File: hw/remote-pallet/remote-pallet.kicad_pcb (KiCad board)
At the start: 2 copper layers, 90 x 90 mm, 85 parts, among them J1 Power, M0 E-MATCH, M1 E-MATCH, M2 E-MATCH, M3 E-MATCH, M4 E-MATCH, M5 E-MATCH, M6 E-MATCH, M7 E-MATCH, Q1 EMatch Test, Q10 Q_PMOS_DGS, Q11 Q_NMOS_DGS, Q12 Q_PMOS_DGS, Q13 Q_NMOS_DGS, Q14 Q_PMOS_DGS, Q15 Q_NMOS_DGS, Q16 Q_PMOS_DGS, Q17 Q_NMOS_DGS, Q2 Q_PMOS_DGS, Q3 Q_NMOS_DGS, Q4 Q_PMOS_DGS, Q5 Q_NMOS_DGS, Q6 Q_PMOS_DGS, Q7 Q_NMOS_DGS, Q8 Q_PMOS_DGS, Q9 Q_NMOS_DGS, SW1 Power, SW2 Arm Hardware, U1 Photon Power, U2 PHOTON, U3 Armed Sense

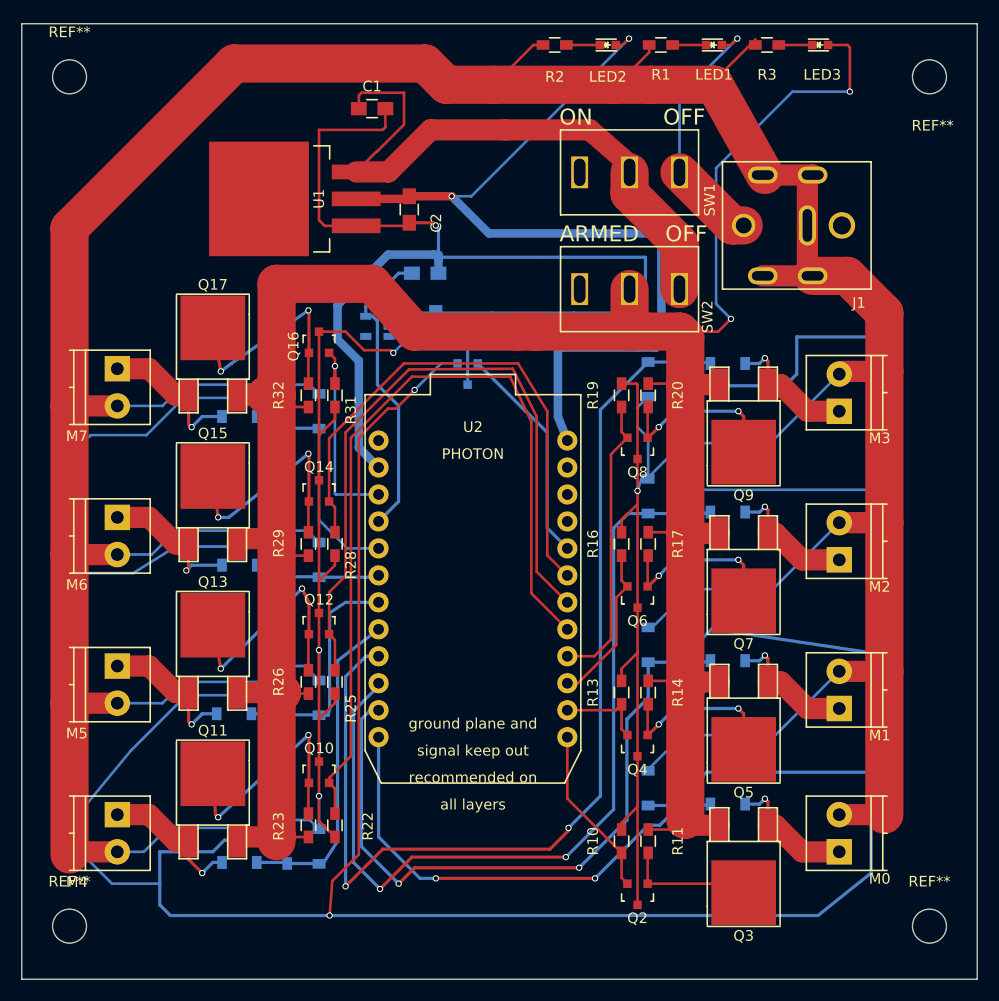
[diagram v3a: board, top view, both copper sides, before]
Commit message: adding graphic and small updates to PCB
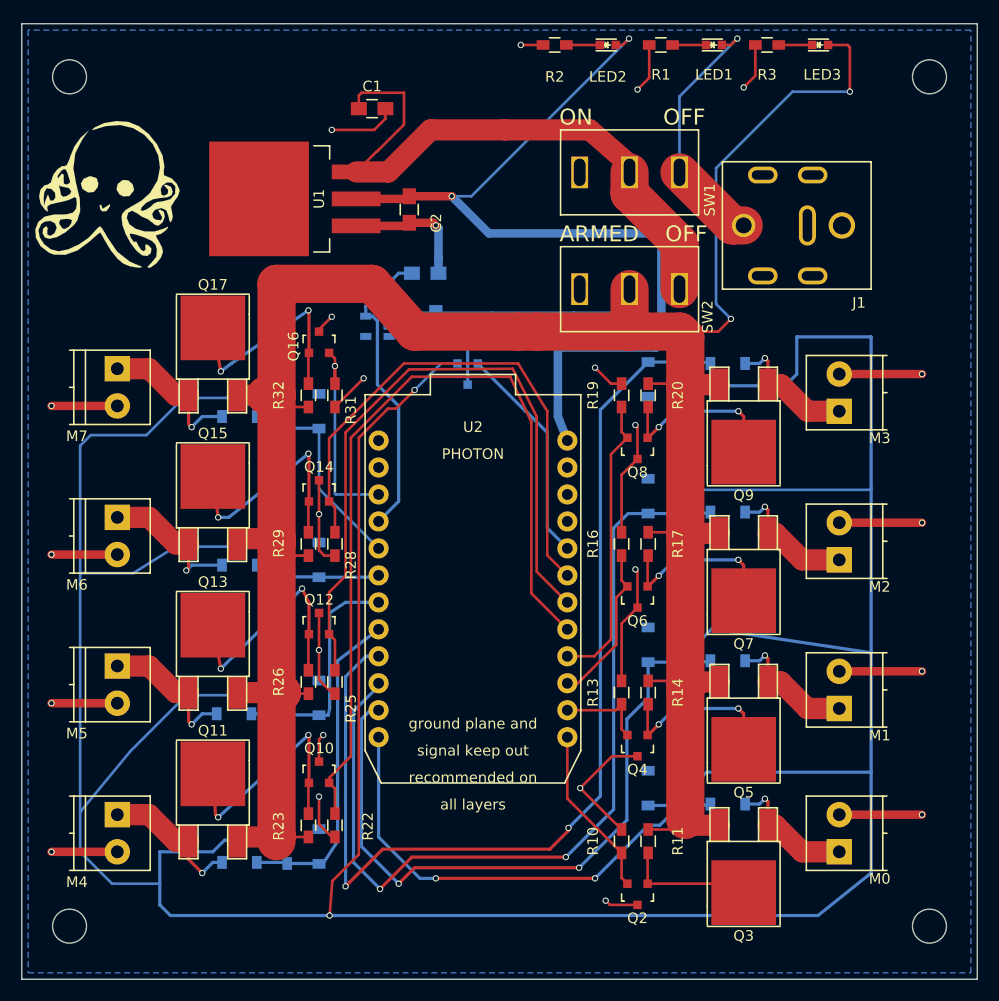
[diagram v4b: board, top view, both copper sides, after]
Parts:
- added G***: LOGO, octopus:octopus, F.Cu at (99.8, 66.2)
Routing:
- net GND: track 678.2 -> 158.5 mm, vias 5 -> 24
- net Sense7: track 21.7 -> 19.9 mm
- added copper zone on B.Cu, net GND

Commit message: updating pcb and adding part numbers for digikey
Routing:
- net GND: track 158.5 -> 234.7 mm, vias 24 -> 32
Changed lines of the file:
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@@
     (thickness 1.6)
     (drawings 10)
-    (tracks 567)
+    (tracks 597)
     (zones 0)
     (modules 86)
@@
   (segment (start 121.5 83.9) (end 121.5 81.55076) (width 0.25) (layer F.Cu) (net 30))
   (segment (start 121.5 81.55076) (end 120.95 81.00076) (width 0.25) (layer F.Cu) (net 30))
+  (segment (start 169 83) (end 169 80.1) (width 0.8) (layer F.Cu) (net 31) (status 400000))
+  (via (at 176.8 79.8) (size 0.6) (drill 0.4) (layers F.Cu B.Cu) (net 31))
+  (segment (start 169.3 79.8) (end 176.8 79.8) (width 0.8) (layer F.Cu) (net 31))
+  (segment (start 169 80.1) (end 169.3 79.8) (width 0.8) (layer F.Cu) (net 31))
+  (segment (start 169 97) (end 169 94.4) (width 0.8) (layer F.Cu) (net 31) (status 400000))
+  (via (at 176.8 94.3) (size 0.6) (drill 0.4) (layers F.Cu B.Cu) (net 31))
+  (segment (start 169.1 94.3) (end 176.8 94.3) (width 0.8) (layer F.Cu) (net 31))
+  (segment (start 169 94.4) (end 169.1 94.3) (width 0.8) (layer F.Cu) (net 31))
+  (segment (start 169 111) (end 169 107.5) (width 0.8) (layer F.Cu) (net 31) (status 400000))
+  (via (at 176.8 107.2) (size 0.6) (drill 0.4) (layers F.Cu B.Cu) (net 31))
+  (segment (start 169.3 107.2) (end 176.8 107.2) (width 0.8) (layer F.Cu) (net 31))
+  (segment (start 169 107.5) (end 169.3 107.2) (width 0.8) (layer F.Cu) (net 31))
+  (segment (start 169 124.5) (end 169 122.2) (width 0.8) (layer F.Cu) (net 31) (status 400000))
+  (via (at 176.8 121.9) (size 0.6) (drill 0.4) (layers F.Cu B.Cu) (net 31))
+  (segment (start 169.3 121.9) (end 176.8 121.9) (width 0.8) (layer F.Cu) (net 31))
+  (segment (start 169 122.2) (end 169.3 121.9) (width 0.8) (layer F.Cu) (net 31))
+  (segment (start 101 86) (end 101 88.1) (width 0.8) (layer F.Cu) (net 31) (status 400000))
+  (via (at 94.8 88.3) (size 0.6) (drill 0.4) (layers F.Cu B.Cu) (net 31))
+  (segment (start 100.8 88.3) (end 94.8 88.3) (width 0.8) (layer F.Cu) (net 31))
+  (segment (start 101 88.1) (end 100.8 88.3) (width 0.8) (layer F.Cu) (net 31))
+  (segment (start 101 100) (end 101 102.5) (width 0.8) (layer F.Cu) (net 31) (status 400000))
+  (via (at 94.8 102.4) (size 0.6) (drill 0.4) (layers F.Cu B.Cu) (net 31))
+  (segment (start 100.9 102.4) (end 94.8 102.4) (width 0.8) (layer F.Cu) (net 31))
+  (segment (start 101 102.5) (end 100.9 102.4) (width 0.8) (layer F.Cu) (net 31))
+  (segment (start 101 114) (end 101 116) (width 0.8) (layer F.Cu) (net 31) (status 400000))
+  (via (at 94.8 116) (size 0.6) (drill 0.4) (layers F.Cu B.Cu) (net 31))
+  (segment (start 101 116) (end 94.8 116) (width 0.8) (layer F.Cu) (net 31))
+  (segment (start 101 128) (end 101 129.8) (width 0.8) (layer F.Cu) (net 31) (status 400000))
+  (via (at 94.8 129.8) (size 0.6) (drill 0.4) (layers F.Cu B.Cu) (net 31))
+  (segment (start 101 129.8) (end 94.8 129.8) (width 0.8) (layer F.Cu) (net 31))
+  (segment (start 101 128) (end 94.8 128) (width 0.8) (layer F.Cu) (net 31))
+  (via (at 94.8 128) (size 0.6) (drill 0.4) (layers F.Cu B.Cu) (net 31))
   (segment (start 101 86) (end 94.8 86) (width 0.8) (layer F.Cu) (net 31))
   (via (at 94.8 86) (size 0.6) (drill 0.4) (layers F.Cu B.Cu) (net 31))
@@
   (segment (start 101 114) (end 94.8 114) (width 0.8) (layer F.Cu) (net 31))
   (via (at 94.8 114) (size 0.6) (drill 0.4) (layers F.Cu B.Cu) (net 31))
-  (segment (start 101 128) (end 94.8 128) (width 0.8) (layer F.Cu) (net 31))
-  (via (at 94.8 128) (size 0.6) (drill 0.4) (layers F.Cu B.Cu) (net 31))
   (segment (start 120 79.00178) (end 120 78.8) (width 0.25) (layer F.Cu) (net 31))
   (segment (start 120 78.8) (end 121.2 77.6) (width 0.25) (layer F.Cu) (net 31))

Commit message: updating schematic and PCB
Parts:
- added C5: 100pF, Capacitors_SMD:C_0805_HandSoldering, F.Cu at (152.8, 117.4)
- 3.3V1: renamed from LED2; value 3.3 -> Yellow
- Armed1: renamed from LED3; value Armed -> Green
- Battery1: renamed from LED1; value Battery -> Red
- C3: value 0.47uF -> 10uF; moved to F.Cu
- C4, Q1, U3: moved to F.Cu
- Q10, Q12, Q14, R22, R23, R25, R26, R28, R29: moved to B.Cu
- Q11, Q13, Q15, Q17, Q3, Q5, Q7, Q9: value Q_NMOS_DGS -> Q_NMOS_GDS
- moved R2 86.8 mm to (168.2, 134.8), turned to 0 degrees
- moved R1 86.3 mm to (168.2, 136.8), turned to 0 degrees
- moved J1 85.5 mm to (121.8, 138.2), turned to 90 degrees
- moved Battery1 85.1 mm to (164.4, 136.8), turned to 180 degrees
- moved 3.3V1 84.6 mm to (164.4, 134.8), turned to 180 degrees
- moved R3 81.0 mm to (168.2, 132.8), turned to 0 degrees
- moved Armed1 80.8 mm to (164.4, 132.8), turned to 180 degrees
- moved SW1 69.1 mm to (134.8, 131.6), turned to 180 degrees
- moved G*** 64.8 mm to (49.0, 106.4)
- moved Q2 62.1 mm to (147.4, 70.0), turned to 270 degrees
- moved R23 61.5 mm to (151.4, 73.2), turned to 180 degrees
- moved R22 58.2 mm to (151.4, 75.6), turned to 0 degrees
- moved C1 58.1 mm to (152.8, 109.0), turned to 270 degrees
- moved R10 58.1 mm to (151.4, 69.0), turned to 0 degrees
- moved SW2 56.7 mm to (145.6, 131.6), turned to 180 degrees
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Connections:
- Q1 pad 1: VCCsense -> SenseSwitch
- Q1 pad 2: SenseSwitch -> 3.3V
- Q1 pad 3: 3.3V -> VCCsense
- Q10 pad 1: Net-(Q10-Pad1) -> Fire4
- Q10 pad 2: Fire4 -> GND
- Q10 pad 3: GND -> Net-(Q10-Pad3)
- Q11 pad 1: /ematch-4/EMATCH_VCC -> Net-(Q10-Pad3)
- Q11 pad 2: Net-(Q10-Pad1) -> /ematch-4/EMATCH_VCC
- Q12 pad 1: Net-(Q12-Pad1) -> Fire5
- Q12 pad 2: Fire5 -> GND
- Q12 pad 3: GND -> Net-(Q12-Pad3)
- Q13 pad 1: /ematch-5/EMATCH_VCC -> Net-(Q12-Pad3)
- Q13 pad 2: Net-(Q12-Pad1) -> /ematch-5/EMATCH_VCC
- Q14 pad 1: Net-(Q14-Pad1) -> Fire6
- Q14 pad 2: Fire6 -> GND
- Q14 pad 3: GND -> Net-(Q14-Pad3)
- Q15 pad 1: /ematch-6/EMATCH_VCC -> Net-(Q14-Pad3)
- Q15 pad 2: Net-(Q14-Pad1) -> /ematch-6/EMATCH_VCC
- Q16 pad 1: Net-(Q16-Pad1) -> Fire7
- Q16 pad 2: Fire7 -> GND
- Q16 pad 3: GND -> Net-(Q16-Pad3)
- Q17 pad 1: /ematch-7/EMATCH_VCC -> Net-(Q16-Pad3)
- Q17 pad 2: Net-(Q16-Pad1) -> /ematch-7/EMATCH_VCC
- Q2 pad 1: Net-(Q2-Pad1) -> Fire0
- Q2 pad 2: Fire0 -> GND
- Q2 pad 3: GND -> Net-(Q2-Pad3)
- Q3 pad 1: /ematch-0/EMATCH_VCC -> Net-(Q2-Pad3)
- Q3 pad 2: Net-(Q2-Pad1) -> /ematch-0/EMATCH_VCC
- Q4 pad 1: Net-(Q4-Pad1) -> Fire1
- Q4 pad 2: Fire1 -> GND
- Q4 pad 3: GND -> Net-(Q4-Pad3)
- Q5 pad 1: /ematch-1/EMATCH_VCC -> Net-(Q4-Pad3)
- Q5 pad 2: Net-(Q4-Pad1) -> /ematch-1/EMATCH_VCC
- Q6 pad 1: Net-(Q6-Pad1) -> Fire2
- Q6 pad 2: Fire2 -> GND
- Q6 pad 3: GND -> Net-(Q6-Pad3)
- Q7 pad 1: /ematch-2/EMATCH_VCC -> Net-(Q6-Pad3)
- Q7 pad 2: Net-(Q6-Pad1) -> /ematch-2/EMATCH_VCC
- Q8 pad 1: Net-(Q8-Pad1) -> Fire3
- Q8 pad 2: Fire3 -> GND
- Q8 pad 3: GND -> Net-(Q8-Pad3)
- Q9 pad 1: /ematch-3/EMATCH_VCC -> Net-(Q8-Pad3)
- Q9 pad 2: Net-(Q8-Pad1) -> /ematch-3/EMATCH_VCC
- R11 pad 2: Net-(Q2-Pad1) -> Net-(Q2-Pad3)
- R14 pad 2: Net-(Q4-Pad1) -> Net-(Q4-Pad3)
- R17 pad 2: Net-(Q6-Pad1) -> Net-(Q6-Pad3)
- R20 pad 2: Net-(Q8-Pad1) -> Net-(Q8-Pad3)
- R23 pad 2: Net-(Q10-Pad1) -> Net-(Q10-Pad3)
- R26 pad 2: Net-(Q12-Pad1) -> Net-(Q12-Pad3)
- R29 pad 2: Net-(Q14-Pad1) -> Net-(Q14-Pad3)
- R32 pad 2: Net-(Q16-Pad1) -> Net-(Q16-Pad3)
- U2 pad 13: Fire0 -> Fire6
- U2 pad 14: Fire1 -> Fire5
- U2 pad 15: Fire2 -> Fire4
- U2 pad 16: Fire3 -> Fire0
- U2 pad 17: Fire4 -> Fire1
- U2 pad 18: Fire5 -> Fire2
- U2 pad 19: Fire6 -> Fire3
- U3 pad 3: (no net) -> /ematch-0/VCC
- U3 pad 4: (no net) -> Net-(C5-Pad1)
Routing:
- net VCCsense: track 385.7 -> 23.8 mm, vias 2 -> 8
- net GND: track 234.7 -> 0.00 mm, vias 32 -> 0
- net Net-(Q10-Pad3): track 0.00 -> 96.5 mm, vias 0 -> 1
- net Sense3: track 100.0 -> 13.3 mm, vias 2 -> 0
- net Net-(Q12-Pad3): track 0.00 -> 76.4 mm, vias 0 -> 1
- net 3.3V: track 95.8 -> 169.4 mm, vias 2 -> 1
- net Net-(Q14-Pad3): track 0.00 -> 70.8 mm, vias 0 -> 1
- net Sense2: track 82.7 -> 13.6 mm, vias 2 -> 0
- net Fire4: track 79.5 -> 11.4 mm
- net Net-(Q2-Pad3): track 0.00 -> 61.2 mm, vias 0 -> 2
- net Fire5: track 65.2 -> 9.93 mm
- net Sense1: track 64.5 -> 13.4 mm, vias 2 -> 0
- net Net-(Q4-Pad3): track 0.00 -> 49.5 mm, vias 0 -> 2
- net Fire6: track 51.3 -> 8.82 mm
- net Net-(Q6-Pad3): track 0.00 -> 38.3 mm, vias 0 -> 2
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- removed copper zone on B.Cu, net GND

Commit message: updaint schematic and layout
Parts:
- moved SW1 8.60 mm to (126.2, 131.8)
- moved J1 8.60 mm to (113.2, 138.4)
- moved SW2 8.40 mm to (137.2, 131.8)
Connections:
- U2 pad 20: SenseSwitch -> Armed
- U2 pad 4: Armed -> SenseSwitch
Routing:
- net /ematch-3/EMATCH_VCC: track 7.85 -> 101.9 mm, vias 0 -> 1
- net /ematch-2/EMATCH_VCC: track 7.65 -> 79.9 mm, vias 0 -> 1
- net /ematch-7/EMATCH_VCC: track 7.45 -> 79.5 mm, vias 0 -> 1
- net Armed: track 3.24 -> 71.7 mm, vias 0 -> 1
- net /ematch-6/EMATCH_VCC: track 7.65 -> 68.7 mm, vias 0 -> 1
- net 12V: track 16.8 -> 75.0 mm
- net /ematch-1/EMATCH_VCC: track 7.65 -> 58.8 mm, vias 0 -> 1
- net /ematch-5/EMATCH_VCC: track 7.65 -> 57.3 mm, vias 0 -> 1
- net 3.3V: track 169.4 -> 218.9 mm, vias 1 -> 2
- net SenseSwitch: track 0.00 -> 48.5 mm
- net Sense5: track 13.4 -> 53.7 mm, vias 0 -> 1
- net Sense6: track 13.4 -> 53.4 mm, vias 0 -> 1
- net Sense7: track 12.9 -> 52.9 mm, vias 0 -> 1
- net Sense1: track 13.4 -> 52.9 mm, vias 0 -> 1
- net Sense2: track 13.6 -> 52.9 mm, vias 0 -> 1
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- added copper zone on B.Cu, net GND
- added copper zone on F.Cu, net GND
